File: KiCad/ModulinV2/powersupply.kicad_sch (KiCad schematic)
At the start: 51 parts, among them IC26 L7812CD2T-TR, IC27 NCP5500DADJR2G, IC28 NCP5500DADJR2G, IC29 NCP5500DADJR2G, IC31 LM2576S-12_NOPB, IC32 L7812CD2T-TR, IC36 LM2576S-12_NOPB, IC37 NCP5500DADJR2G, J9 PJ-002B, Q2 DMP610DL-7

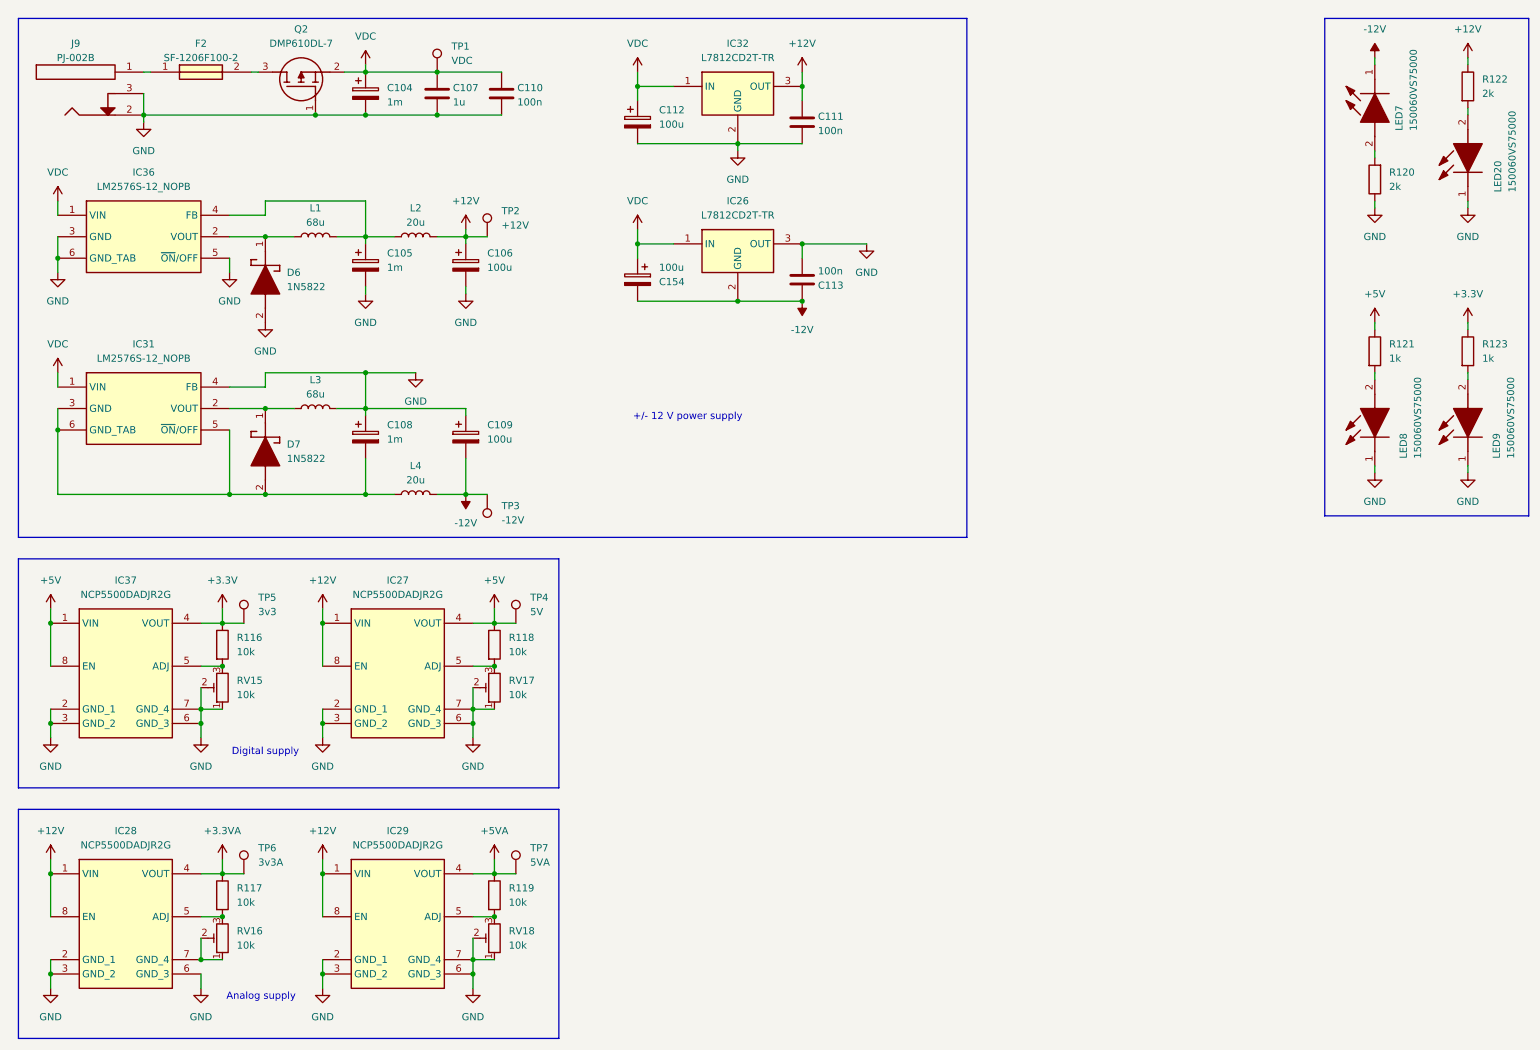
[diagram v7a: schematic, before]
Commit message: Changed switch for the boot and nrst. Fixed the GATE interface trigger
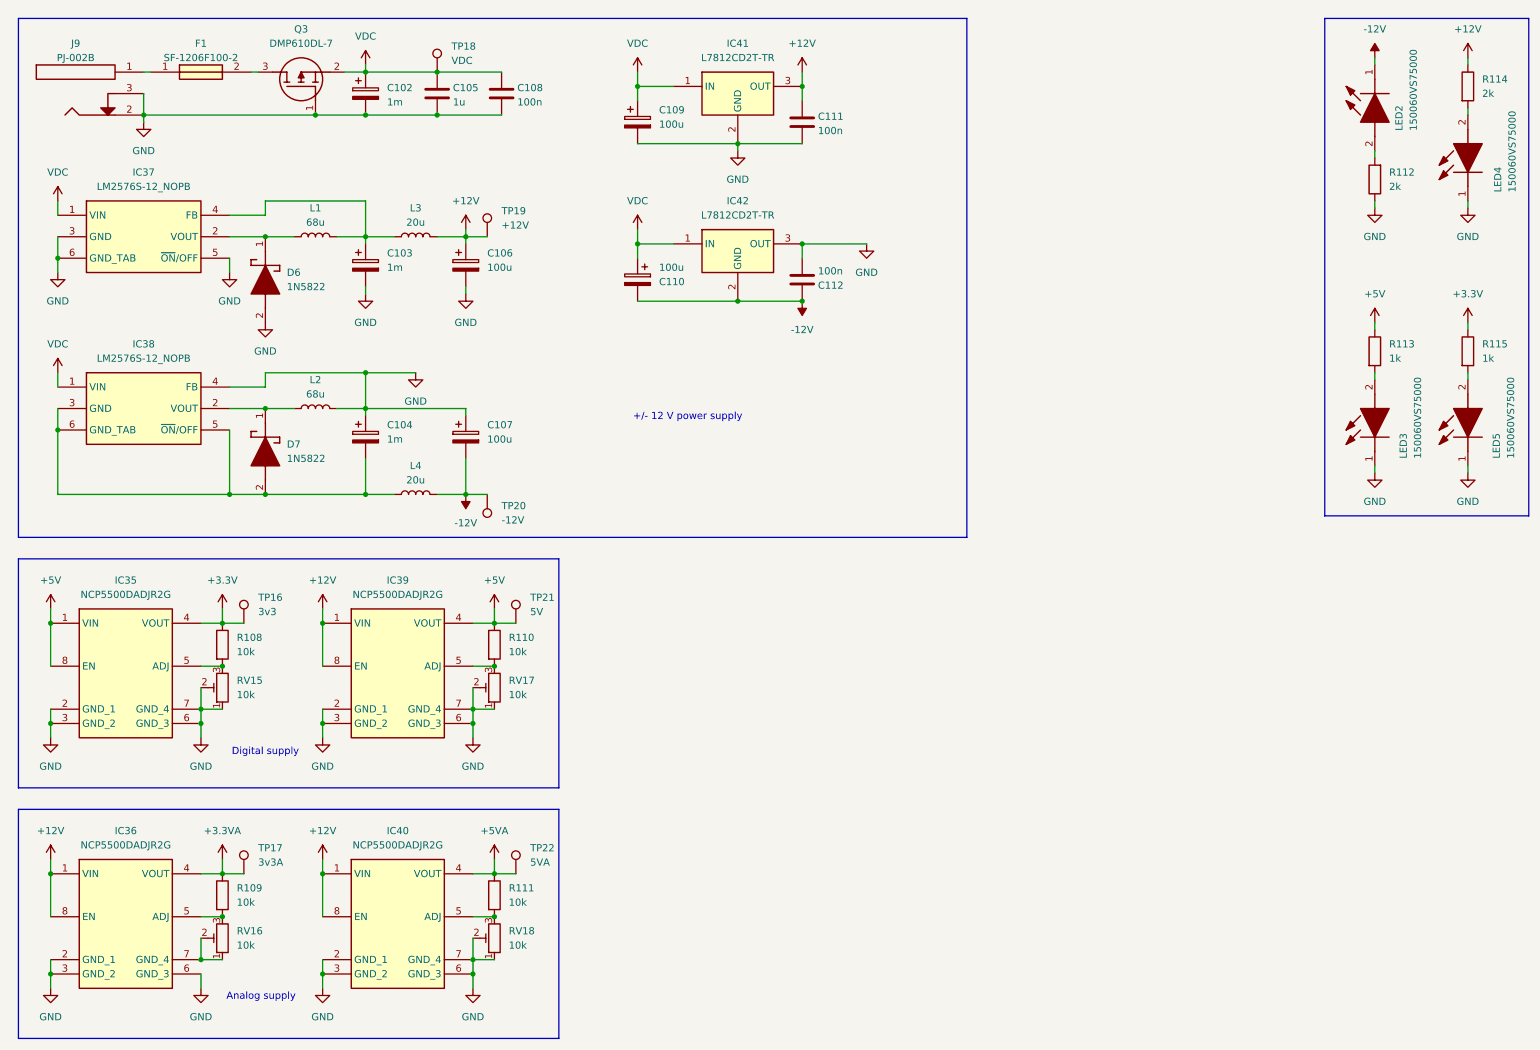
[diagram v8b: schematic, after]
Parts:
- renumbered C104 to C102, C105 to C103, C108 to C104, C107 to C105, C109 to C107, C110 to C108, C112 to C109, C154 to C110, C113 to C112, F2 to F1, IC37 to IC35, IC28 to IC36, IC36 to IC37, IC31 to IC38, IC27 to IC39, IC29 to IC40, IC32 to IC41, IC26 to IC42, L3 to L2, L2 to L3, LED7 to LED2, LED8 to LED3, LED20 to LED4, LED9 to LED5, Q2 to Q3, R116 to R108, R117 to R109, R118 to R110, R119 to R111, R120 to R112, R121 to R113, R122 to R114, R123 to R115, TP5 to TP16, TP6 to TP17, TP1 to TP18, TP2 to TP19, TP3 to TP20, TP4 to TP21, TP7 to TP22
